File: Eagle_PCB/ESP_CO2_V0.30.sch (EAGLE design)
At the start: 38 parts, among them Q1 SI2305CDS, Q2 BSS131, Q5 BSS138, U1 ESP-WROOM-03, U10 SOUND-DETECTOR-INMP441, U2 WIRELESS-LORA-RFM95W#SMD, U3 PCA9548A, U6 SON, U7 MIC5239S, U8 TEMP-HUM-PRES-BME280H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

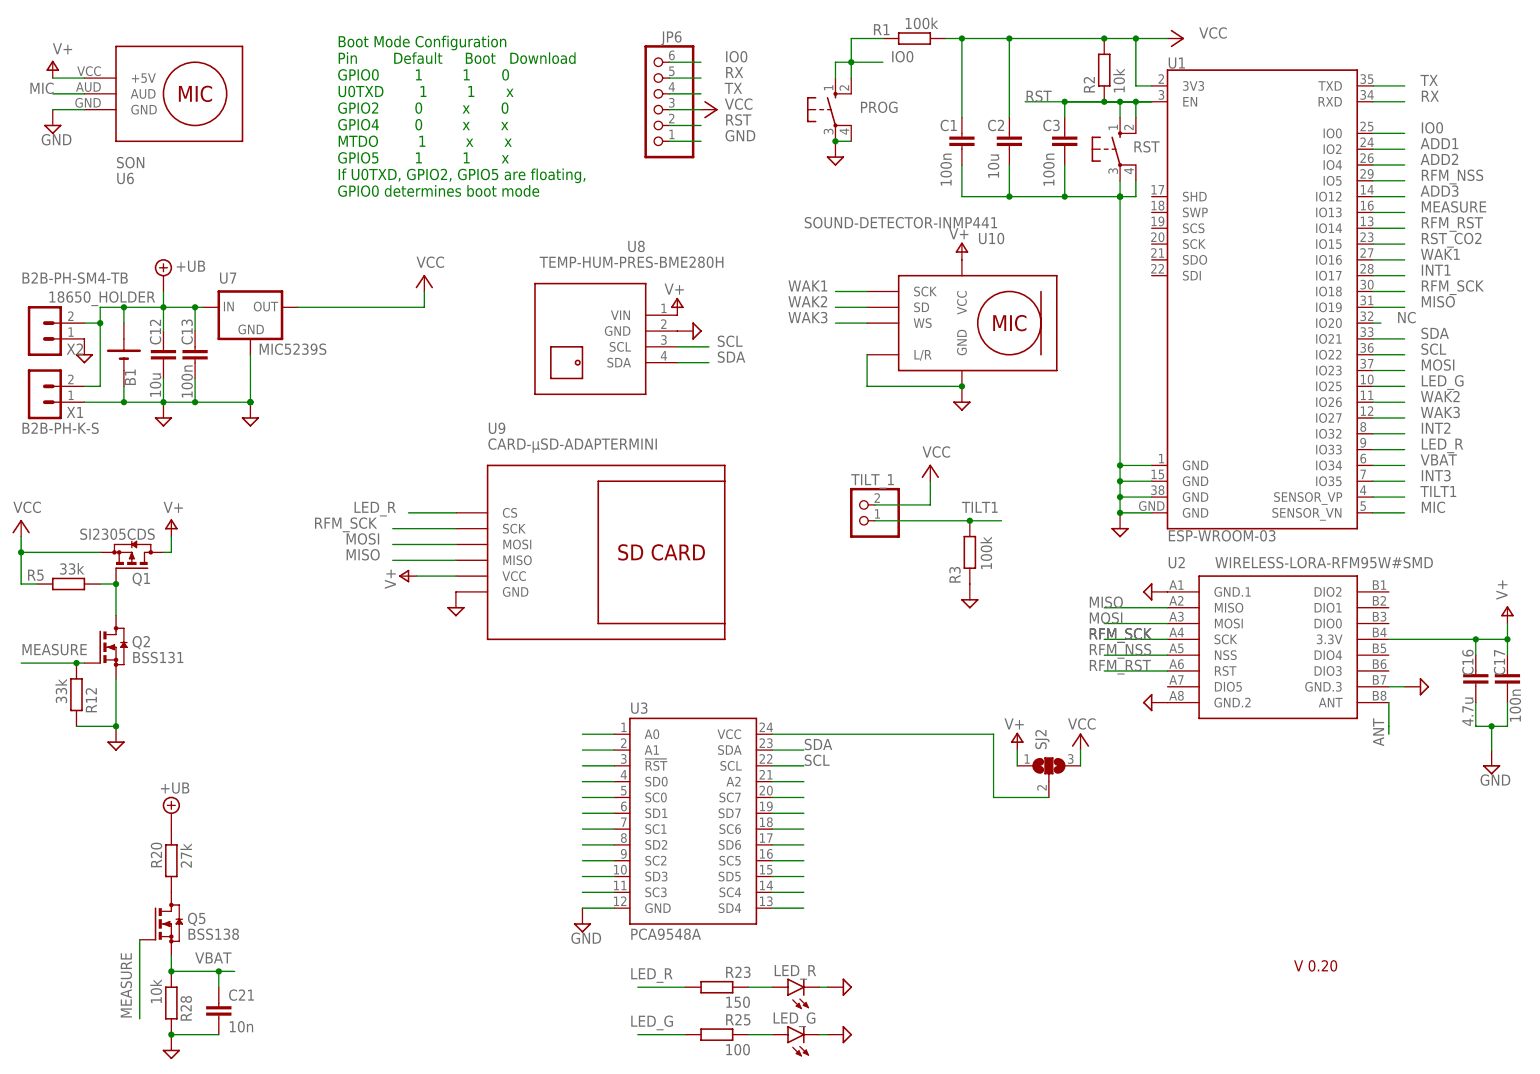
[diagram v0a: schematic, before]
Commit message: Seance du 16/02/2024
J'ai reussi a faire fonctioner les 3 capteurs sur la carte dev ESP32, carte grille, nouveau schematique
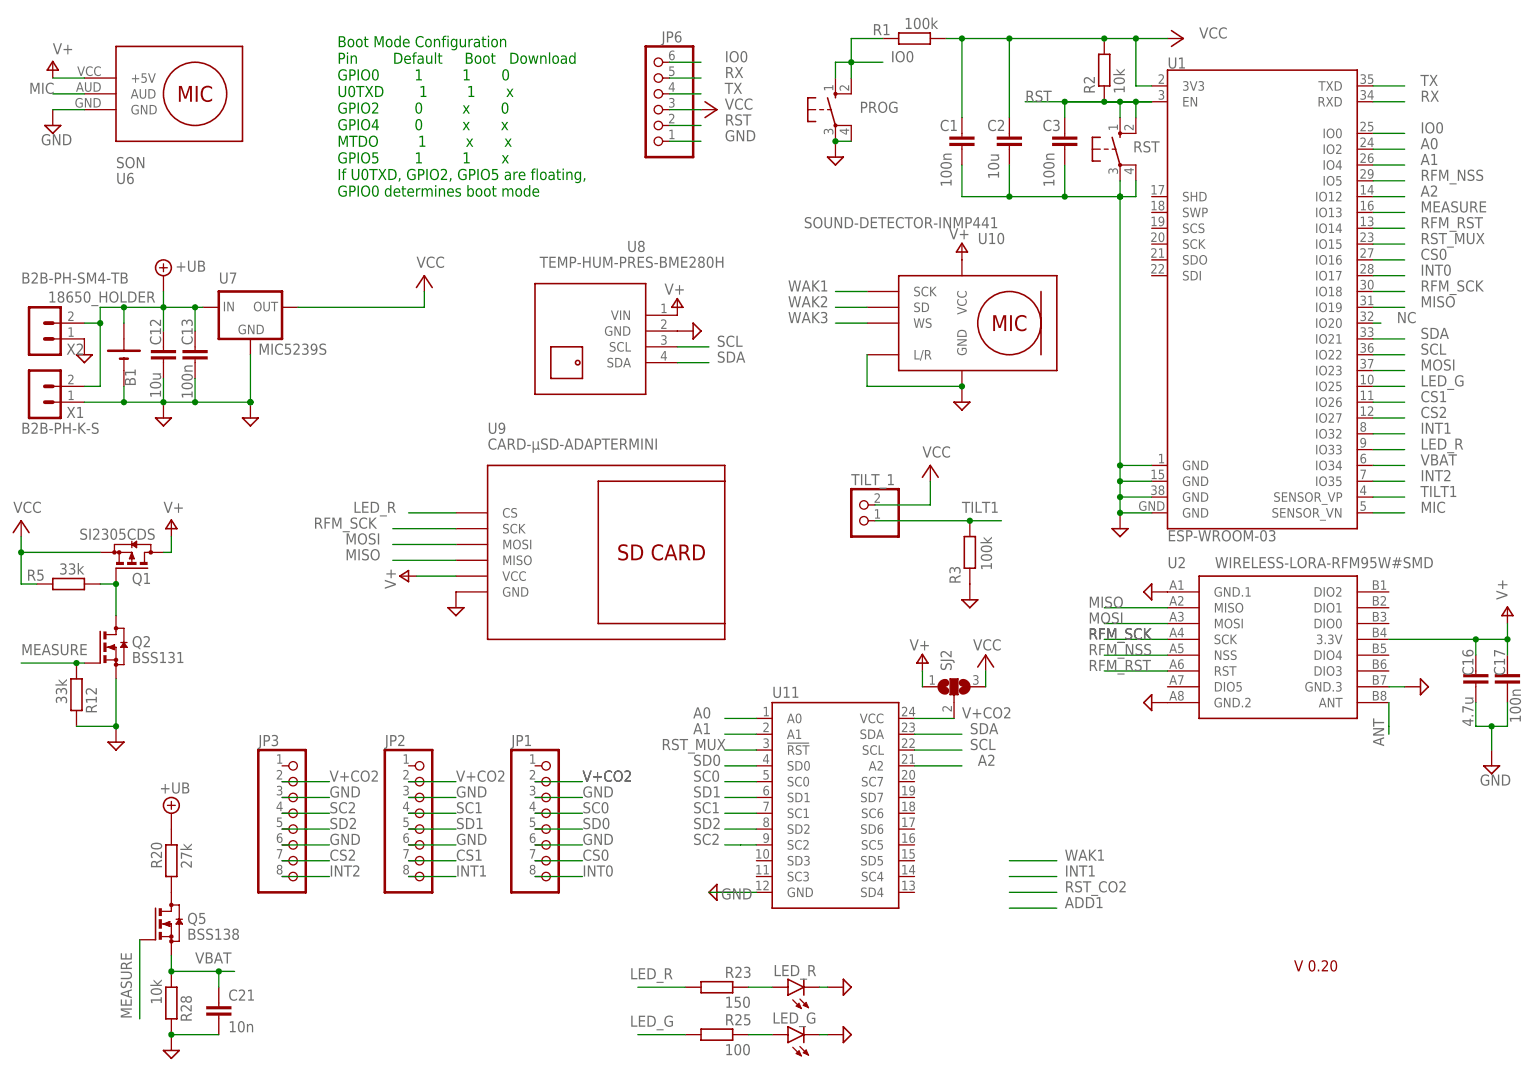
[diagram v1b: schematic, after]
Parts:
- removed U3: PCA9548A, SparkFun-IC-Logic (1):PCA9548A
- added JP1, JP2, JP3: (no value), pinhead:PINHD-1X8
- added U11: PCA9548A, SparkFun-IC-Logic (1):PCA9548A
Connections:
- removed net ADD1: U1.IO2
- removed net ADD2: U1.IO4
- removed net ADD3: U1.IO12
- removed net INT3: U1.IO35
- removed net N$10: U3.SD7
- removed net N$11: U3.SC6
- removed net N$12: U3.SD6
- removed net N$13: U3.SC5
- removed net N$14: U3.SD5
- removed net N$15: U3.SC4
- removed net N$16: U3.SD4
- removed net N$17: U3.A0
- removed net N$18: U3.A1
- removed net N$19: U3.!RST
- removed net N$2: SJ2.2, U3.VCC
- removed net N$20: U3.SD0
- removed net N$21: U3.SC0
- removed net N$22: U3.SD1
- removed net N$23: U3.SC1
- removed net N$24: U3.SD2
- removed net N$25: U3.SC2
- removed net N$26: U3.SD3
- removed net N$27: U3.SC3
- removed net N$6: U3.A2
- removed net N$9: U3.SC7
- removed net RST_CO2: U1.IO15
- new net A0: U1.IO2, U11.A0
- new net A1: U1.IO4, U11.A1
- new net A2: U1.IO12, U11.A2
- new net CS0: JP1.7, U1.IO16
- new net CS1: JP2.7, U1.IO26
- new net CS2: JP3.7, U1.IO27
- new net INT0: JP1.8, U1.IO17
- new net RST_MUX: U1.IO15, U11.!RST
- new net SC0: JP1.4, U11.SC0
- new net SC1: JP2.4, U11.SC1
- new net SC2: JP3.4, U11.SC2
- new net SD0: JP1.5, U11.SD0
- new net SD1: JP2.5, U11.SD1
- new net SD2: JP3.5, U11.SD2
- new net V+CO2: JP1.2, JP2.2, JP3.2, SJ2.2, U11.VCC
- net GND: now also JP1.3, JP1.6, JP2.3, JP2.6, JP3.3, JP3.6, U11.GND; no longer U3.GND
- net INT1: now also JP2.8, U1.IO32; no longer U1.IO17
- net INT2: now also JP3.8, U1.IO35; no longer U1.IO32
- net SCL: now also U11.SCL; no longer U3.SCL
- net SDA: now also U11.SDA; no longer U3.SDA
- net WAK1: no longer U1.IO16
- net WAK2: no longer U1.IO26
- net WAK3: no longer U1.IO27
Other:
- moved on the sheet: SJ2
